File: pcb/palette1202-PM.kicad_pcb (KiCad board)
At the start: 2 copper layers, 100 x 86.8 mm, 45 parts, among them J10 BAT+, J11 BAT-, J4 OLED, SW1 SW_PUSH, SW10 SW_PUSH, SW11 SW_PUSH, SW12 SW_PUSH, SW2 SW_PUSH, SW20 SW_RESET, SW21 PWR, SW3 SW_PUSH, SW4 SW_PUSH, SW5 SW_PUSH, SW6 SW_PUSH, SW7 SW_PUSH, SW8 SW_PUSH, SW9 SW_PUSH, U2 ProMicro

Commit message: updated main board
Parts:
- added C11: 100u, Capacitor_Tantalum_SMD:CP_EIA-3216-10_Kemet-I_Pad1.58x1.35mm_HandSolder, F.Cu at (162.8, 38.1)
- added J20: BAT+, nilgiri:Hole 0.8mm, F.Cu at (89.8, 39.5)
- added J21: BAT-, nilgiri:Hole 0.8mm, F.Cu at (89.8, 54.7)
- added JP100: LEFT-A1, Jumper:SolderJumper-2_P1.3mm_Open_TrianglePad1.0x1.5mm, B.Cu at (176.9, 62.8)
- added JP101: LEFT-B1, Jumper:SolderJumper-2_P1.3mm_Open_TrianglePad1.0x1.5mm, B.Cu at (172.0, 62.8)
- added JP110: RIGHT-B1, Jumper:SolderJumper-2_P1.3mm_Open_TrianglePad1.0x1.5mm, F.Cu at (176.9, 62.8)
- added JP111: RIGHT-A1, Jumper:SolderJumper-2_P1.3mm_Open_TrianglePad1.0x1.5mm, F.Cu at (172.0, 62.8)
- added JP120: LEFT-A2, Jumper:SolderJumper-2_P1.3mm_Open_TrianglePad1.0x1.5mm, B.Cu at (177.0, 78.3)
- added JP121: LEFT-B2, Jumper:SolderJumper-2_P1.3mm_Open_TrianglePad1.0x1.5mm, B.Cu at (172.0, 78.3)
- added JP130: RIGHT-B2, Jumper:SolderJumper-2_P1.3mm_Open_TrianglePad1.0x1.5mm, F.Cu at (177.0, 78.3)
- added JP131: RIGHT-A2, Jumper:SolderJumper-2_P1.3mm_Open_TrianglePad1.0x1.5mm, F.Cu at (172.0, 78.3)
- added JP200: LEFT-SDA, Jumper:SolderJumper-2_P1.3mm_Open_TrianglePad1.0x1.5mm, B.Cu at (123.6, 50.1)
- added JP201: LEFT-SCL, Jumper:SolderJumper-2_P1.3mm_Open_TrianglePad1.0x1.5mm, B.Cu at (123.6, 47.6)
- added JP202: LEFT-VCC, Jumper:SolderJumper-2_P1.3mm_Open_TrianglePad1.0x1.5mm, B.Cu at (123.6, 45.1)
- added JP203: LEFT-GND, Jumper:SolderJumper-2_P1.3mm_Open_TrianglePad1.0x1.5mm, B.Cu at (123.6, 42.5)
- added JP210: RIGHT-SDA, Jumper:SolderJumper-2_P1.3mm_Open_TrianglePad1.0x1.5mm, F.Cu at (123.6, 42.5)
- added JP211: RIGHT-SCL, Jumper:SolderJumper-2_P1.3mm_Open_TrianglePad1.0x1.5mm, F.Cu at (123.6, 45.1)
- added JP212: RIGHT-VCC, Jumper:SolderJumper-2_P1.3mm_Open_TrianglePad1.0x1.5mm, F.Cu at (123.6, 47.6)
- added JP213: RIGHT-GND, Jumper:SolderJumper-2_P1.3mm_Open_TrianglePad1.0x1.5mm, F.Cu at (123.6, 50.1)
- added JP220: VCC-USB, Jumper:SolderJumper-2_P1.3mm_Open_TrianglePad1.0x1.5mm, F.Cu at (95.1, 45.4)
- added JP221: VCC-BAT, Jumper:SolderJumper-2_P1.3mm_Open_TrianglePad1.0x1.5mm, F.Cu at (95.1, 48.7)
- added SW22: PWR, Button_Switch_SMD:SW_SPDT_PCM12, B.Cu at (155.2, 37.7)
- D1, D10, D11, D12, D2, D3, D4, D5, D6, D7, D8, D9: footprint nilgiri:D3_TH_SMD -> kbd:D3_TH_SMD
- D13: renamed from D20; footprint nilgiri:D3_TH_SMD -> kbd:D3_TH_SMD
- D14: renamed from D21; footprint nilgiri:D3_TH_SMD -> kbd:D3_TH_SMD
- D30: renamed from D32; footprint Keebio:D_SOD123F -> kbd:D3_SMD
- D31: footprint Keebio:D_SOD123F -> kbd:D3_SMD
- SW1, SW10, SW11, SW12, SW2, SW3, SW4, SW5, SW6, SW7, SW8, SW9: footprint nilgiri:CherryMX_Choc_Hotswap-1Side -> nilgiri:CherryMX_Choc_Hotswap
- U2: footprint kbd:ProMicro_v3 -> kbd:ProMicro_v2
- moved D10 24.1 mm to (138.0, 99.2), turned to 180 degrees
- moved D12 23.7 mm to (163.6, 94.9)
- moved D2 17.0 mm to (94.7, 110.6), turned to 180 degrees
- moved D11 14.0 mm to (156.8, 105.2), turned to 180 degrees
- moved C10 13.8 mm to (162.8, 38.1), turned to 0 degrees
- moved D8 13.8 mm to (138.0, 105.4), turned to 180 degrees
- moved D5 13.4 mm to (119.0, 105.9), turned to 180 degrees
- moved D3 11.1 mm to (119.0, 81.7), turned to 180 degrees
- moved D30 9.67 mm to (157.4, 53.2), turned to 180 degrees
- moved D1 8.87 mm to (99.9, 91.3), turned to 180 degrees
- moved D31 8.72 mm to (157.4, 50.9), turned to 180 degrees
- moved D7 7.02 mm to (138.0, 96.0), turned to 180 degrees
- moved D4 6.99 mm to (119.0, 100.9), turned to 180 degrees
- moved D6 6.59 mm to (138.0, 76.8), turned to 180 degrees
- moved D9 6.48 mm to (157.0, 86.0), turned to 180 degrees
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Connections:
- net Net-(C10-Pad1) renamed Vbat
- EC1 pad A: RA1 -> Net-(EC1-PadA)
- EC1 pad B: RB1 -> Net-(EC1-PadB)
- EC2 pad A: RA2 -> Net-(EC2-PadA)
- EC2 pad B: RB2 -> Net-(EC2-PadB)
- J4 pad 1: SDA -> Net-(J4-Pad1)
- J4 pad 2: SCL -> Net-(J4-Pad2)
- J4 pad 3: VCC -> Net-(J4-Pad3)
- J4 pad 4: GND -> Net-(J4-Pad4)
- U2 pad 1: (no net) -> Net-(U2-Pad1)
- U2 pad 16: (no net) -> Net-(U2-Pad16)
- U2 pad 2: (no net) -> Net-(U2-Pad2)
- U2 pad 24: (no net) -> Net-(U2-Pad24)
- U2 pad 7: (no net) -> Net-(U2-Pad7)
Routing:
- net GND: track 26.8 -> 127.8 mm, vias 0 -> 4
- net Row1: track 121.9 -> 182.5 mm
- net Col3: track 98.9 -> 155.0 mm, vias 0 -> 5
- net Col2: track 86.3 -> 139.2 mm, vias 0 -> 5
- net Row0: track 104.5 -> 154.8 mm
- net Col1: track 82.8 -> 131.8 mm, vias 0 -> 4
- net Vbat: track 77.5 -> 117.9 mm, vias 1 -> 3
- net Net-(D10-Pad2): track 17.0 -> 54.1 mm, vias 0 -> 2
- net Net-(JP202-Pad1): track 0.00 -> 33.4 mm, vias 0 -> 1
- net Col0: track 76.5 -> 106.9 mm, vias 0 -> 3
- net RB1: track 73.7 -> 102.0 mm, vias 0 -> 1
- net Net-(D12-Pad2): track 28.1 -> 56.2 mm, vias 0 -> 1
- net Col4: track 110.7 -> 137.5 mm, vias 0 -> 2
- net RA1: track 79.1 -> 103.2 mm, vias 0 -> 1
- net Net-(D11-Pad2): track 16.2 -> 35.3 mm, vias 0 -> 1
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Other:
- board size 100 x 86.8 mm -> 100 x 88.3 mm
- board text added: "OLED"
- board text added: "PME / v2.30(200330)"
- board text added: "RESET"
- board text removed: "PME / v0.90(191124)"

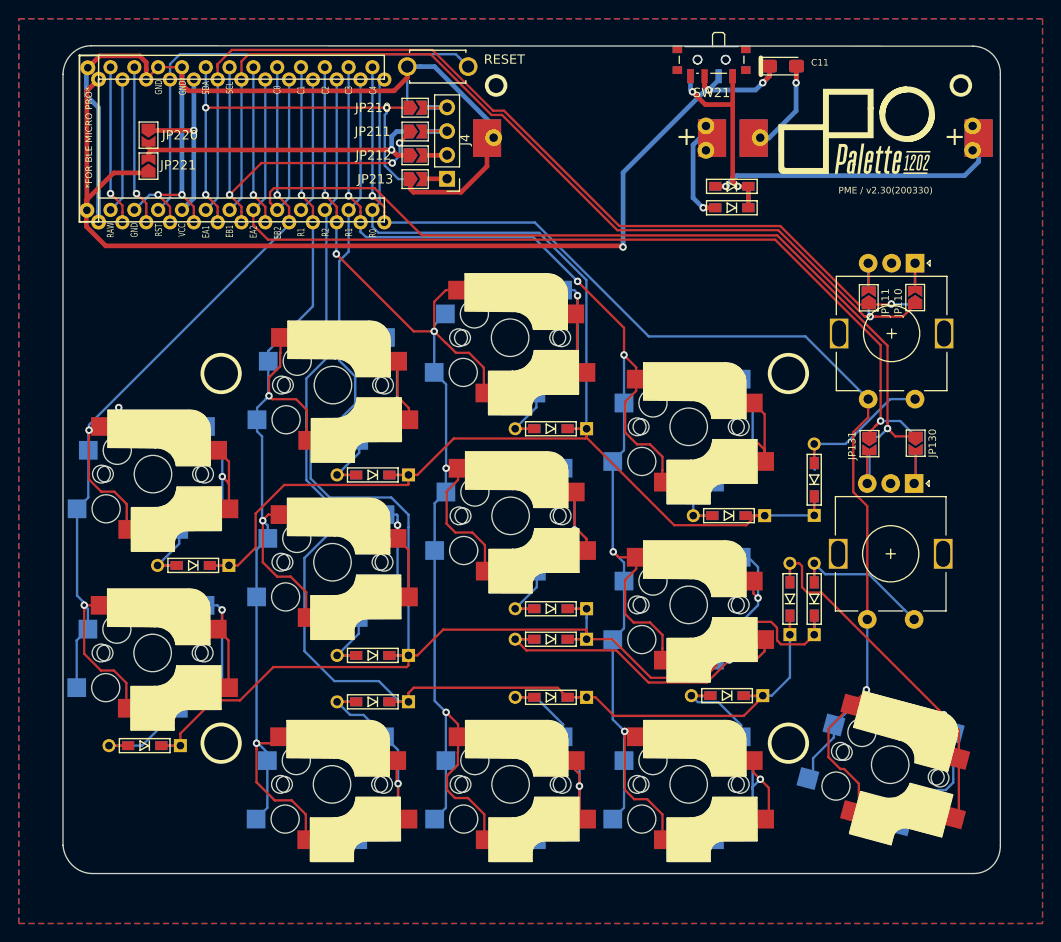
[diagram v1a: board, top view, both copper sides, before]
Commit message: added connecter for split layout(testing)
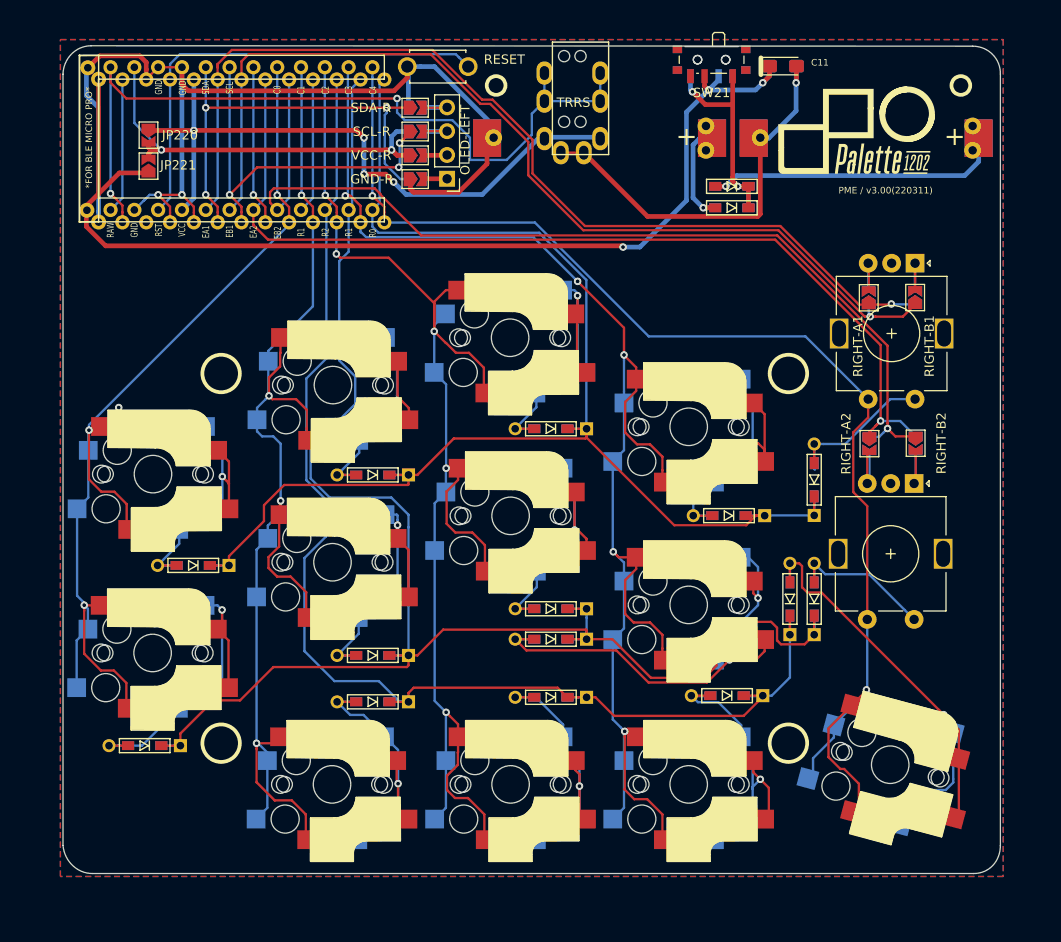
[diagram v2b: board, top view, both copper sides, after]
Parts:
- added J1: MJ-4PP-9, kbd:MJ-4PP-9, F.Cu at (141.2, 35.5)
- renumbered JP203 to GND-L, JP213 to GND-R, J4 to OLED-LEFT, JP201 to SCL-L, JP211 to SCL-R, JP200 to SDA-L, JP210 to SDA-R, JP202 to VCC-L, JP212 to VCC-R
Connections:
- JP220 pad 2: Net-(JP202-Pad1) -> LEFT
- JP221 pad 2: Net-(JP202-Pad1) -> LEFT
- SW21 pad 3: (no net) -> unconnected-(SW21-Pad3)
- SW22 pad 3: (no net) -> unconnected-(SW22-Pad3)
- U2 pad 1: Net-(U2-Pad1) -> DATA
- U2 pad 16: Net-(U2-Pad16) -> unconnected-(U2-Pad16)
- U2 pad 2: Net-(U2-Pad2) -> LEFT
- U2 pad 24: Net-(U2-Pad24) -> unconnected-(U2-Pad24)
- U2 pad 7: Net-(U2-Pad7) -> unconnected-(U2-Pad7)
- VCC-L pad 1: Net-(JP202-Pad1) -> LEFT
- VCC-R pad 1: Net-(JP202-Pad1) -> LEFT
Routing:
- net DATA: track 0.00 -> 86.5 mm, vias 0 -> 2
- net VCC: track 19.3 -> 70.4 mm, vias 1 -> 4
- net LEFT: track 0.00 -> 43.5 mm, vias 0 -> 2
- net Net-(JP202-Pad1): track 33.4 -> 0.00 mm, vias 1 -> 0
- net GND: track 127.8 -> 160.1 mm
- net Net-(U2-Pad2): track 17.4 -> 0.00 mm, vias 1 -> 0
- net unconnected-(U2-Pad7): track 0.00 -> 17.1 mm, vias 0 -> 1
- net Net-(U2-Pad7): track 17.1 -> 0.00 mm, vias 1 -> 0
- net Net-(U2-Pad1): track 17.1 -> 0.00 mm, vias 1 -> 0
- net unconnected-(U2-Pad16): track 0.00 -> 14.4 mm
- net Net-(U2-Pad16): track 14.4 -> 0.00 mm
- net unconnected-(U2-Pad24): track 0.00 -> 14.4 mm
- net Net-(U2-Pad24): track 14.4 -> 0.00 mm
- net RA1: track 103.2 -> 105.4 mm
- net Col1: track 131.8 -> 133.9 mm
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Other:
- net class Default removed
- board text added: "OLED-RIGHT"
- board text added: "PME / v3.00(220311)"
- board text removed: "OLED"
- board text removed: "PME / v2.30(200330)"

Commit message: minor fix, etc.
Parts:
- JP220: value VCC-USB -> OLED-USB
- JP221: value VCC-BAT -> OLED-BAT
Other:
- board text added: "PME / v3.10(221214)"
- board text removed: "PME / v3.00(220311)"
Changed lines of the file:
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@@
     (fp_line (start -3 -1.75) (end -3 -1.5) (layer "F.SilkS") (width 0.15))
     (fp_line (start -3 1.75) (end 3 1.75) (layer "F.SilkS") (width 0.15))
-    (pad "1" thru_hole circle locked (at 3.25 0 180) (size 2 2) (drill 1.3) (layers *.Cu "F.SilkS" "B.Mask")
+    (pad "1" thru_hole circle locked (at 3.25 0 180) (size 2 2) (drill 1.3) (layers *.Cu "B.Mask")
       (net 1 "GND") (pinfunction "1") (pintype "passive"))
-    (pad "2" thru_hole circle locked (at -3.25 0 180) (size 2 2) (drill 1.3) (layers *.Cu "F.SilkS" "B.Mask")
+    (pad "2" thru_hole circle locked (at -3.25 0 180) (size 2 2) (drill 1.3) (layers *.Cu "B.Mask")
       (net 16 "RESET") (pinfunction "2") (pintype "passive"))
   )
@@
     (property "Sheetname" "")
     (attr exclude_from_pos_files)
-    (fp_text reference "JP221" (at 0.1002 3.162324 180) (layer "F.SilkS")
+    (fp_text reference "JP221" (at 0.1002 3.162324 180) (layer "F.SilkS") hide
       (effects (font (size 1 1) (thickness 0.15)))
     )
-    (fp_text value "VCC-BAT" (at 0 1.9 90) (layer "F.Fab")
+    (fp_text value "OLED-BAT" (at -0.0268 4.953 180) (layer "F.SilkS")
       (effects (font (size 1 1) (thickness 0.15)))
     )
@@
     (property "Sheetname" "")
     (attr exclude_from_pos_files)
-    (fp_text reference "JP220" (at 0.0014 -3.3528 180) (layer "F.SilkS")
+    (fp_text reference "JP220" (at 0.0014 -3.3528 180) (layer "F.SilkS") hide
       (effects (font (size 1 1) (thickness 0.15)))
     )
-    (fp_text value "VCC-USB" (at 0 1.9 90) (layer "F.Fab")
+    (fp_text value "OLED-USB" (at 0 -5.207 180) (layer "F.SilkS")
       (effects (font (size 1 1) (thickness 0.15)))
     )
@@
     (effects (font (size 0.7 0.7) (thickness 0.15)))
   )
-  (gr_text "PME / v3.00(220311)" (at 178.7906 51.3334) (layer "F.SilkS")
+  (gr_text "PME / v3.10(221214)" (at 178.7906 51.3334) (layer "F.SilkS")
     (effects (font (size 0.7 0.7) (thickness 0.15)) (justify right))
   )
@@
     (effects (font (size 2.997199 2.697479) (thickness 0.374649)) (justify left bottom))
   )
+  (dimension (type aligned) (layer "B.Cu")
+    (pts (xy 85.598 36.321999) (xy 186.182 36.321999))
+    (height -7.873999)
+    (gr_text "100.5840 mm" (at 135.89 26.648) (layer "B.Cu")
+      (effects (font (size 1.5 1.5) (thickness 0.3)))
+    )
+    (format (units 3) (units_format 1) (precision 4))
+    (style (thickness 0.2) (arrow_length 1.27) (text_position_mode 0) (extension_height 0.58642) (extension_offset 0.5) keep_text_aligned)
+  )
   (dimension (type aligned) (layer "F.Fab")
-    (pts (xy 89.5096 56.1594) (xy 89.5096 124.079))
-    (height 13.843)
-    (gr_text "67.9196 mm" (at 74.5166 90.1192 90) (layer "F.Fab")
+    (pts (xy 86.233 35.306) (xy 86.233 124.46))
+    (height 10.668)
+    (gr_text "89.1540 mm" (at 71.755 79.6925 90) (layer "F.Fab")
       (effects (font (size 1 1) (thickness 0.15)))
     )
     (format (units 2) (units_format 1) (precision 4))
-    (style (thickness 0.15) (arrow_length 1.27) (text_position_mode 0) (extension_height 0.58642) (extension_offset 0) keep_text_aligned)
+    (style (thickness 0.15) (arrow_length 1.27) (text_position_mode 2) (extension_height 0.58642) (extension_offset 0) keep_text_aligned)
   )
   (segment (start 98.692 51.804838) (end 98.692 51.804838) (width 0.25) (layer "F.Cu") (net 1))
